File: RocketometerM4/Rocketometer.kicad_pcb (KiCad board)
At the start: 2 copper layers, 35.6 x 20.3 mm, 30 parts, among them J001 USB_OTG, J301 Battery_Cell_Conn, J401 CONN_01X06, J701 Micro_SD_Card_SPI, U201 MIC5319-3.3, U301 MCP73831, U401 TM4C1232, Y440 Crystal_GND24

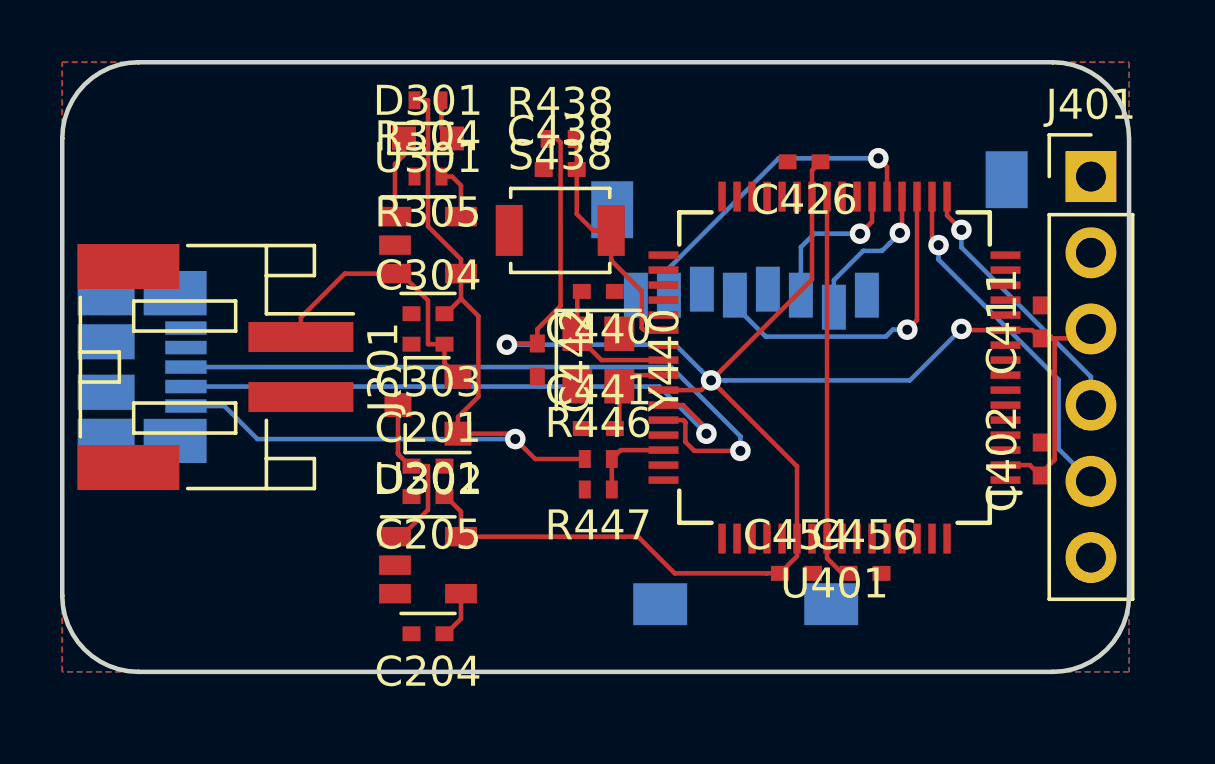
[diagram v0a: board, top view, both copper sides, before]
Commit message: Added switch footprint
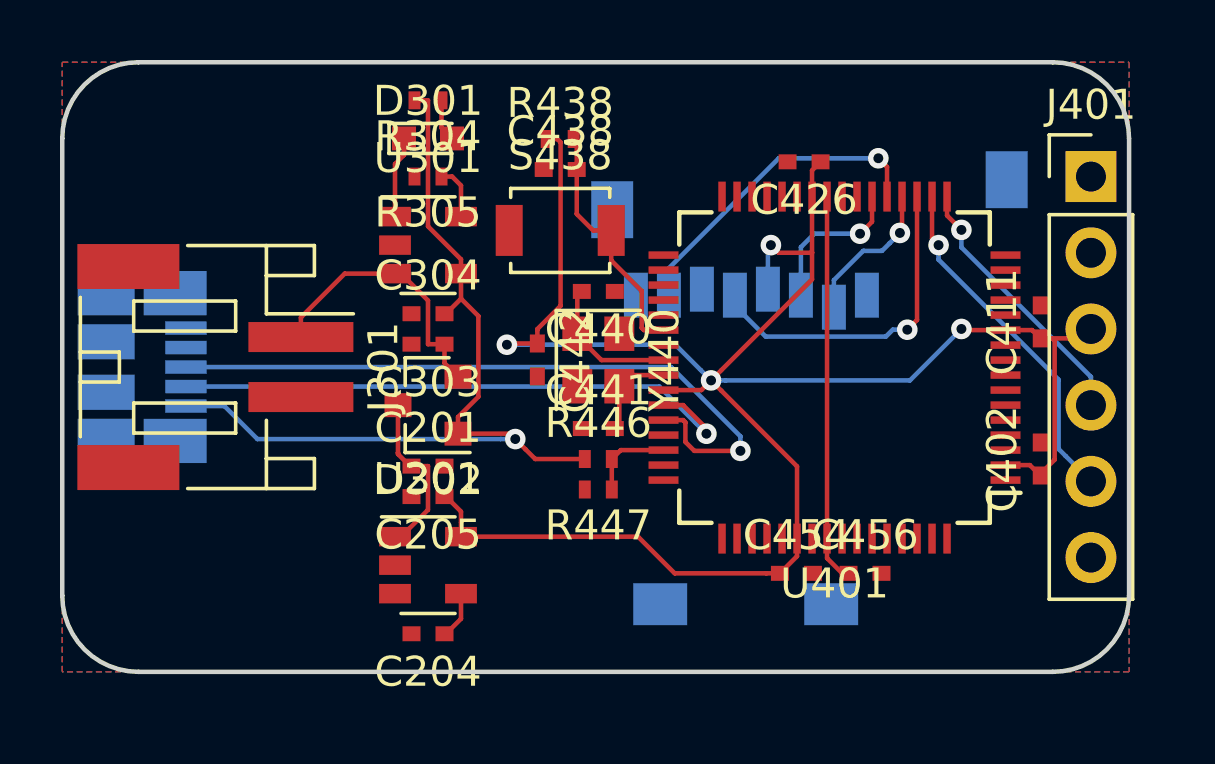
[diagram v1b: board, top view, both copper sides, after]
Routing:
- net +3V3: track 67.1 -> 70.1 mm, vias 3 -> 4
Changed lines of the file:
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@@
-(kicad_pcb (version 4) (host pcbnew 4.0.6-e0-6349~52~ubuntu16.10.1)
+(kicad_pcb (version 4) (host pcbnew 4.0.6-e0-6349~53~ubuntu16.04.1)
   (general
     (links 85)
-    (no_connects 5)
-    (area -43.255001 -12.775001 -7.544999 7.695001)
+    (no_connects 0)
+    (area -44.4024 -15.188201 -3.904266 8.6474)
     (thickness 1.6)
     (drawings 8)
-    (tracks 185)
+    (tracks 191)
     (zones 0)
     (modules 30)
@@
   (segment (start -31.883 3.114) (end -32.088 3.114) (width 0.1524) (layer F.Cu) (net 1))
   (segment (start -31.538 0.762) (end -30.988 0.762) (width 0.1524) (layer F.Cu) (net 1))
+  (segment (start -18.18691 -6.35) (end -19.304 -6.35) (width 0.1524) (layer F.Cu) (net 3))
+  (segment (start -19.6584 -6.5036) (end -19.6584 -5.1342) (width 0.1524) (layer B.Cu) (net 3) (status 800000))
+  (segment (start -19.558 -6.604) (end -19.6584 -6.5036) (width 0.1524) (layer B.Cu) (net 3))
+  (via (at -19.558 -6.604) (size 0.6858) (drill 0.3302) (layers F.Cu B.Cu) (net 3))
+  (segment (start -19.304 -6.35) (end -19.558 -6.604) (width 0.1524) (layer F.Cu) (net 3))
   (segment (start -21.066851 -2.094231) (end -21.551784 -2.094231) (width 0.1524) (layer B.Cu) (net 3))
   (segment (start -14.923769 -2.094231) (end -21.066851 -2.094231) (width 0.1524) (layer B.Cu) (net 3))
@@
   (segment (start -26.67851 -10.141962) (end -26.5684 -10.031852) (width 0.1524) (layer F.Cu) (net 3))
   (segment (start -21.894683 -2.43713) (end -21.551784 -2.094231) (width 0.1524) (layer B.Cu) (net 3))
-  (segment (start -18.18691 -8.221962) (end -18.18691 -5.459105) (width 0.1524) (layer F.Cu) (net 3))
+  (segment (start -18.18691 -8.221962) (end -18.18691 -6.35) (width 0.1524) (layer F.Cu) (net 3))
+  (segment (start -18.18691 -6.35) (end -18.18691 -5.459105) (width 0.1524) (layer F.Cu) (net 3))
   (segment (start -18.18691 -5.459105) (end -21.208885 -2.43713) (width 0.1524) (layer F.Cu) (net 3))
   (segment (start -21.208885 -1.751332) (end -21.551784 -2.094231) (width 0.1524) (layer F.Cu) (net 3))
